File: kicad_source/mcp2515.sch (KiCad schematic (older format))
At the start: 15 parts, among them CN4 GH_SM04B-GHS-TB, CN5 GH_SM04B-GHS-TB, U4 MCP2515, U8 MCP2515, U9 SN65HVD232, Y1 16MHz, Y2 16MHz

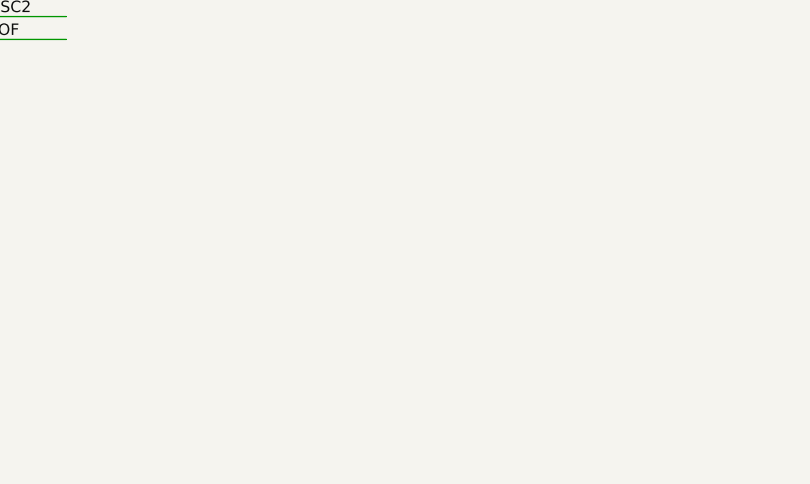
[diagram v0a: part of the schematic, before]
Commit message: added screw terminals for CAN
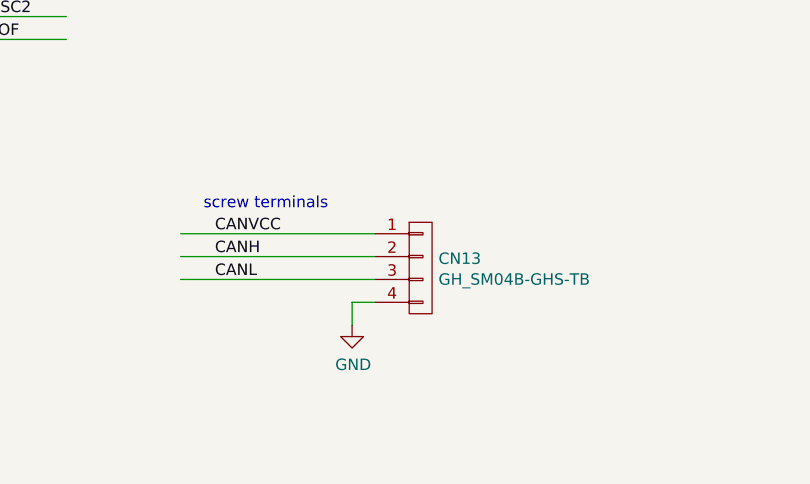
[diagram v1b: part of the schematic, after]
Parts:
- added CN13: GH_SM04B-GHS-TB, CON_wuerth:WR-TBL_691322310004, symbol mechanical-connectors:CONN_01X04
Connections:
- wire segments 88 -> 93
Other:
- note added: "screw terminals"
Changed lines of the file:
@@
 Sheet 2 2
 Title "OpenCyphalPicoBase"
-Date "2022-06-06"
+Date "2022-06-09"
 Rev "dev_0.1"
 Comp "generationmake"
@@
 Wire Wire Line
 	7700 6150 7900 6150
+$Comp
+L mechanical-connectors:CONN_01X04 CN?
+U 1 1 62A340B9
+P 5900 5500
+AR Path="/624F7A5F/62A340B9" Ref="CN?"  Part="1"
+AR Path="/5ED92F9C/62A340B9" Ref="CN13"  Part="1"
+F 0 "CN13" H 5978 5541 50  0000 L CNN
+F 1 "GH_SM04B-GHS-TB" H 5978 5450 50  0000 L CNN
+F 2 "CON_wuerth:WR-TBL_691322310004" H 5900 5500 50  0001 C CNN
+F 3 "" H 5900 5500 50  0000 C CNN
+	1    5900 5500
+	1    0    0    -1
+$EndComp
+Wire Wire Line
+	4850 5450 5700 5450
+Wire Wire Line
+	4850 5550 5700 5550
+Text Label 5000 5450 0    50   ~ 0
+CANH
+Text Label 5000 5550 0    50   ~ 0
+CANL
+$Comp
+L power-supply:GND #PWR?
+U 1 1 62A341BD
+P 5600 5750
+AR Path="/624F7A5F/62A341BD" Ref="#PWR?"  Part="1"
+AR Path="/5ED92F9C/62A341BD" Ref="#PWR055"  Part="1"
+F 0 "#PWR055" H 5600 5500 50  0001 C CNN
+F 1 "GND" H 5605 5577 50  0000 C CNN
+F 2 "" H 5600 5750 50  0000 C CNN
+F 3 "" H 5600 5750 50  0000 C CNN
+	1    5600 5750
+	1    0    0    -1
+$EndComp
+Wire Wire Line
+	5700 5650 5600 5650
+Wire Wire Line
+	5600 5650 5600 5750
+Text Notes 4950 5250 0    50   ~ 0
+screw terminals
+Text Label 5000 5350 0    50   ~ 0
+CANVCC
+Wire Wire Line
+	4850 5350 5700 5350
 $EndSCHEMATC
